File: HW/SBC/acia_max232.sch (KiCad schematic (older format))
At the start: 12 parts, among them J1 Serial Port, U4 MAX232, U5 6551

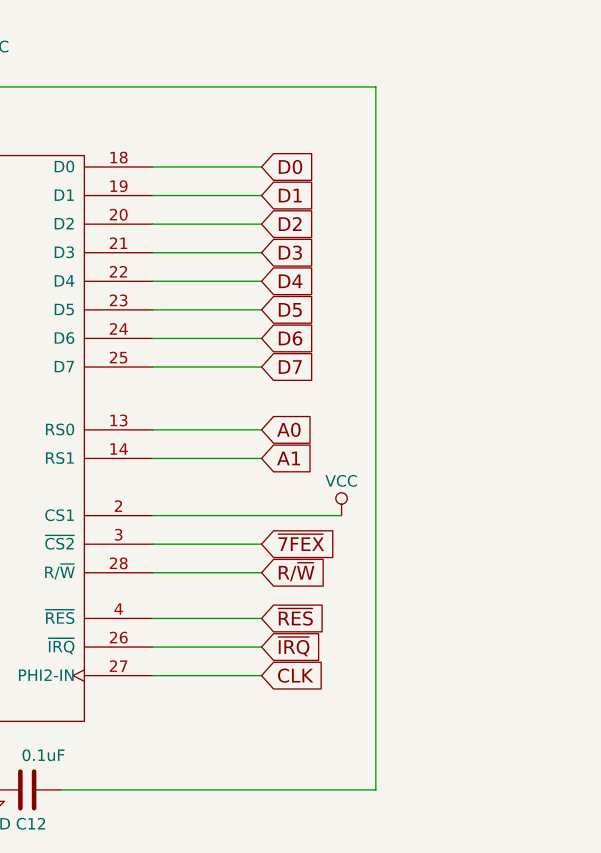
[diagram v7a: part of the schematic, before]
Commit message: New schema. Adding a VIA and sound chip.
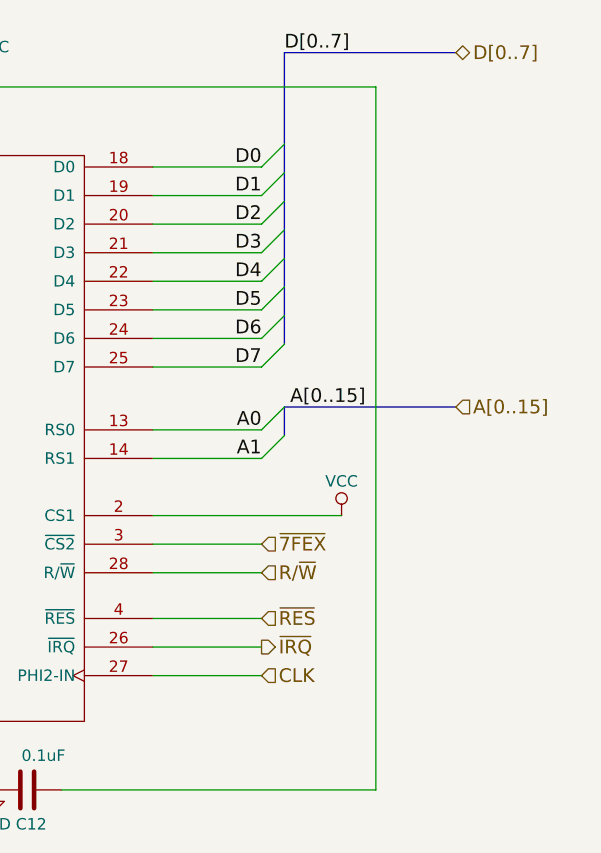
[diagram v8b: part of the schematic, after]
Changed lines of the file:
@@
 LIBS:zetex
 LIBS:Zilog
+LIBS:pluto
 LIBS:pluto-cache
 EELAYER 25 0
@@
 $Descr A4 11693 8268
 encoding utf-8
-Sheet 3 6
+Sheet 3 7
 Title "ACIA, MAX232 and serial port connector"
 Date "2017-03-25"
@@
 	-1   0    0    1
 $EndComp
-Text GLabel 9150 1950 2    60   Input ~ 0
-D0
-Text GLabel 9150 2075 2    60   Input ~ 0
-D1
-Text GLabel 9150 2200 2    60   Input ~ 0
-D2
-Text GLabel 9150 2325 2    60   Input ~ 0
-D3
-Text GLabel 9150 2450 2    60   Input ~ 0
-D4
-Text GLabel 9150 2575 2    60   Input ~ 0
-D5
-Text GLabel 9150 2700 2    60   Input ~ 0
-D6
-Text GLabel 9150 2825 2    60   Input ~ 0
-D7
-Text GLabel 9150 3100 2    60   Input ~ 0
-A0
-Text GLabel 9150 3225 2    60   Input ~ 0
-A1
-$Comp
-L VCC #PWR07
+$Comp
+L VCC #PWR18
 U 1 1 58D6F59A
 P 9500 3475
-F 0 "#PWR07" H 9500 3325 50  0001 C CNN
+F 0 "#PWR18" H 9500 3325 50  0001 C CNN
 F 1 "VCC" H 9500 3625 50  0000 C CNN
 F 2 "" H 9500 3475 50  0001 C CNN
@@
 	1    0    0    -1
 $EndComp
-Text GLabel 9150 3600 2    60   Input ~ 0
-~7FEX
-Text GLabel 9150 3725 2    60   Input ~ 0
-R/~W
 $Comp
 L CRYSTAL XTAL1
@@
 $EndComp
 $Comp
-L GND #PWR08
+L GND #PWR12
 U 1 1 58D7044A
 P 6450 1500
-F 0 "#PWR08" H 6450 1250 50  0001 C CNN
+F 0 "#PWR12" H 6450 1250 50  0001 C CNN
 F 1 "GND" H 6450 1350 50  0000 C CNN
 F 2 "" H 6450 1500 50  0001 C CNN
@@
 	-1   0    0    1
 $EndComp
-Text GLabel 9150 3925 2    60   Input ~ 0
-~RES
-Text GLabel 9150 4050 2    60   Input ~ 0
-~IRQ
-Text GLabel 9150 4175 2    60   Input ~ 0
-CLK
 $Comp
 L CP1_Small C3
@@
 $EndComp
 $Comp
-L GND #PWR09
+L GND #PWR8
 U 1 1 58D716F3
 P 3050 3250
-F 0 "#PWR09" H 3050 3000 50  0001 C CNN
+F 0 "#PWR8" H 3050 3000 50  0001 C CNN
 F 1 "GND" H 3050 3100 50  0000 C CNN
 F 2 "" H 3050 3250 50  0001 C CNN
@@
 $EndComp
 $Comp
-L GND #PWR010
+L GND #PWR7
 U 1 1 58D71F12
 P 1650 3150
-F 0 "#PWR010" H 1650 2900 50  0001 C CNN
+F 0 "#PWR7" H 1650 2900 50  0001 C CNN
 F 1 "GND" H 1650 3000 50  0000 C CNN
 F 2 "" H 1650 3150 50  0001 C CNN
@@
 $EndComp
 $Comp
-L GND #PWR011
+L GND #PWR11
 U 1 1 58D72DB3
 P 4500 4550
-F 0 "#PWR011" H 4500 4300 50  0001 C CNN
+F 0 "#PWR11" H 4500 4300 50  0001 C CNN
 F 1 "GND" H 4500 4400 50  0000 C CNN
 F 2 "" H 4500 4550 50  0001 C CNN
@@
 $EndComp
 $Comp
-L GND #PWR012
+L GND #PWR9
 U 1 1 58D73252
 P 4500 1950
-F 0 "#PWR012" H 4500 1700 50  0001 C CNN
+F 0 "#PWR9" H 4500 1700 50  0001 C CNN
 F 1 "GND" H 4500 1800 50  0000 C CNN
 F 2 "" H 4500 1950 50  0001 C CNN
@@
 NoConn ~ 1825 2450
 $Comp
-L GND #PWR013
+L GND #PWR15
 U 1 1 58D744C7
 P 7275 3925
-F 0 "#PWR013" H 7275 3675 50  0001 C CNN
+F 0 "#PWR15" H 7275 3675 50  0001 C CNN
 F 1 "GND" H 7275 3775 50  0000 C CNN
 F 2 "" H 7275 3925 50  0001 C CNN
@@
 $EndComp
 $Comp
-L GND #PWR014
+L GND #PWR14
 U 1 1 58D74507
 P 7275 3500
-F 0 "#PWR014" H 7275 3250 50  0001 C CNN
+F 0 "#PWR14" H 7275 3250 50  0001 C CNN
 F 1 "GND" H 7275 3350 50  0000 C CNN
 F 2 "" H 7275 3500 50  0001 C CNN
@@
 $EndComp
 $Comp
-L GND #PWR015
+L GND #PWR13
 U 1 1 59019537
 P 7275 1500
-F 0 "#PWR015" H 7275 1250 50  0001 C CNN
+F 0 "#PWR13" H 7275 1250 50  0001 C CNN
 F 1 "GND" H 7275 1350 50  0000 C CNN
 F 2 "" H 7275 1500 50  0001 C CNN
@@
 	3050 4350 4500 4350
 $Comp
-L GND #PWR016
+L GND #PWR17
 U 1 1 5924C9C7
 P 7975 4675
-F 0 "#PWR016" H 7975 4425 50  0001 C CNN
+F 0 "#PWR17" H 7975 4425 50  0001 C CNN
 F 1 "GND" H 7975 4525 50  0000 C CNN
 F 2 "" H 7975 4675 50  0001 C CNN
@@
 $EndComp
 $Comp
-L VCC #PWR017
+L VCC #PWR10
 U 1 1 5924CA70
 P 4500 4350
-F 0 "#PWR017" H 4500 4200 50  0001 C CNN
+F 0 "#PWR10" H 4500 4200 50  0001 C CNN
 F 1 "VCC" V 4500 4525 50  0000 C CNN
 F 2 "" H 4500 4350 50  0001 C CNN
@@
 $EndComp
 $Comp
-L VCC #PWR018
+L VCC #PWR16
 U 1 1 5924CC0E
 P 7975 1600
-F 0 "#PWR018" H 7975 1450 50  0001 C CNN
+F 0 "#PWR16" H 7975 1450 50  0001 C CNN
 F 1 "VCC" H 7975 1775 50  0000 C CNN
 F 2 "" H 7975 1600 50  0001 C CNN
@@
 	1    0    0    -1
 $EndComp
+Text Label 9150 1950 2    60   ~ 0
+D0
+Text Label 9150 2075 2    60   ~ 0
+D1
+Text Label 9150 2200 2    60   ~ 0
+D2
+Text Label 9150 2325 2    60   ~ 0
+D3
+Text Label 9150 2450 2    60   ~ 0
+D4
+Text Label 9150 2575 2    60   ~ 0
+D5
+Text Label 9150 2700 2    60   ~ 0
+D6
+Text Label 9150 2825 2    60   ~ 0
+D7
+Entry Wire Line
+	9150 1950 9250 1850
+Entry Wire Line
+	9150 2075 9250 1975
+Entry Wire Line
+	9150 2200 9250 2100
+Entry Wire Line
+	9150 2325 9250 2225
+Entry Wire Line
+	9150 2450 9250 2350
+Entry Wire Line
+	9150 2575 9250 2475
+Entry Wire Line
+	9150 2700 9250 2600
+Entry Wire Line
+	9150 2825 9250 2725
+Text Label 9150 3100 2    60   ~ 0
+A0
+Text Label 9150 3225 2    60   ~ 0
+A1
+Entry Wire Line
+	9150 3100 9250 3000
+Entry Wire Line
+	9150 3225 9250 3125
+Text HLabel 9150 3600 2    60   Input ~ 0
+~7FEX
+Text HLabel 9150 3725 2    60   Input ~ 0
+R/~W
+Text HLabel 9150 3925 2    60   Input ~ 0
+~RES
+Text HLabel 9150 4050 2    60   Output ~ 0
+~IRQ
+Text HLabel 9150 4175 2    60   Input ~ 0
+CLK
+Wire Bus Line
+	9250 2725 9250 1450
+Wire Bus Line
+	9250 1450 10000 1450
+Text Label 9250 1450 0    60   ~ 0
+D[0..7]
+Text HLabel 10000 1450 2    60   BiDi ~ 0
+D[0..7]
+Wire Bus Line
+	9250 3125 9250 3000
+Wire Bus Line
+	9250 3000 10000 3000
+Text Label 9275 3000 0    60   ~ 0
+A[0..15]
+Text HLabel 10000 3000 2    60   Input ~ 0
+A[0..15]
 $EndSCHEMATC
